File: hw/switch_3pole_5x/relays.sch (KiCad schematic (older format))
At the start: 31 parts, among them J1 WAGO 2081-1123, J2 WAGO 2081-1123, J3 WAGO 2081-1123, J4 WAGO 2081-1123, J5 WAGO 2081-1123, Q1 BSS138, Q2 BSS138, Q3 BSS138, Q4 BSS138, Q5 BSS138

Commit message: Added LED and testpoints
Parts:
- added D10, D6, D7, D8, D9: LED, LED:LED_RM2.54mm_D3mm, symbol standard:LED
- added J10: tp_relay_1, Connector_Miscelleaneus:Testpoint_1mm, symbol connectors:CONN_1
- added J11: tp_relay_2, Connector_Miscelleaneus:Testpoint_1mm, symbol connectors:CONN_1
- added J17: tp_relay_3, Connector_Miscelleaneus:Testpoint_1mm, symbol connectors:CONN_1
- added J18: tp_relay_4, Connector_Miscelleaneus:Testpoint_1mm, symbol connectors:CONN_1
- added J6: tp_relay_0, Connector_Miscelleaneus:Testpoint_1mm, symbol connectors:CONN_1
- added R12, R13, R14, R15, R6: 1k5, Resistor:R_0805, symbol standard:R
- D1, D2, D3, D4, D5: symbol D -> switch_3pole_5x-rescue:D
- J1, J2, J3, J4, J5: symbol CONN_3X1 -> switch_3pole_5x-rescue:CONN_3X1
- LOGO2: symbol OPEN_HARDWARE_1 -> switch_3pole_5x-rescue:OPEN_HARDWARE_1
- Q1, Q2, Q3, Q4, Q5: symbol BSS138 -> switch_3pole_5x-rescue:BSS138
- R1, R10, R11, R2, R3, R4, R5, R7, R8, R9: symbol R -> switch_3pole_5x-rescue:R
- REL1, REL2, REL3, REL4, REL5: symbol FINDER_34.51.7.024 -> switch_3pole_5x-rescue:FINDER_34.51.7.024
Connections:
- net GND: no longer R3.2
- net at D1.1 (A), Q1.3 (D), REL1.1 (+): now also D6.2 (C), J6.1
- net at D2.1 (A), Q2.3 (D), REL2.1 (+): now also D7.2 (C), J10.1
- net at D3.1 (A), Q3.3 (D), REL3.1 (+): now also D8.2 (C), J11.1
- net at D4.1 (A), Q4.3 (D), REL4.1 (+): now also D9.2 (C), J17.1
- net at D5.1 (A), Q5.3 (D), REL5.1 (+): now also D10.2 (C), J18.1
- new net: D6.1 (A), R6.1
- new net: D7.1 (A), R12.1
- new net: D8.1 (A), R13.1
- new net: D9.1 (A), R14.1
- new net: D10.1 (A), R15.1
- new net +5V: R12.2, R13.2, R14.2, R15.2, R6.2
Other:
- moved on the sheet: D1, D2, D3, D4, D5, J1, J2, J3, J4, J5, Q1, Q2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

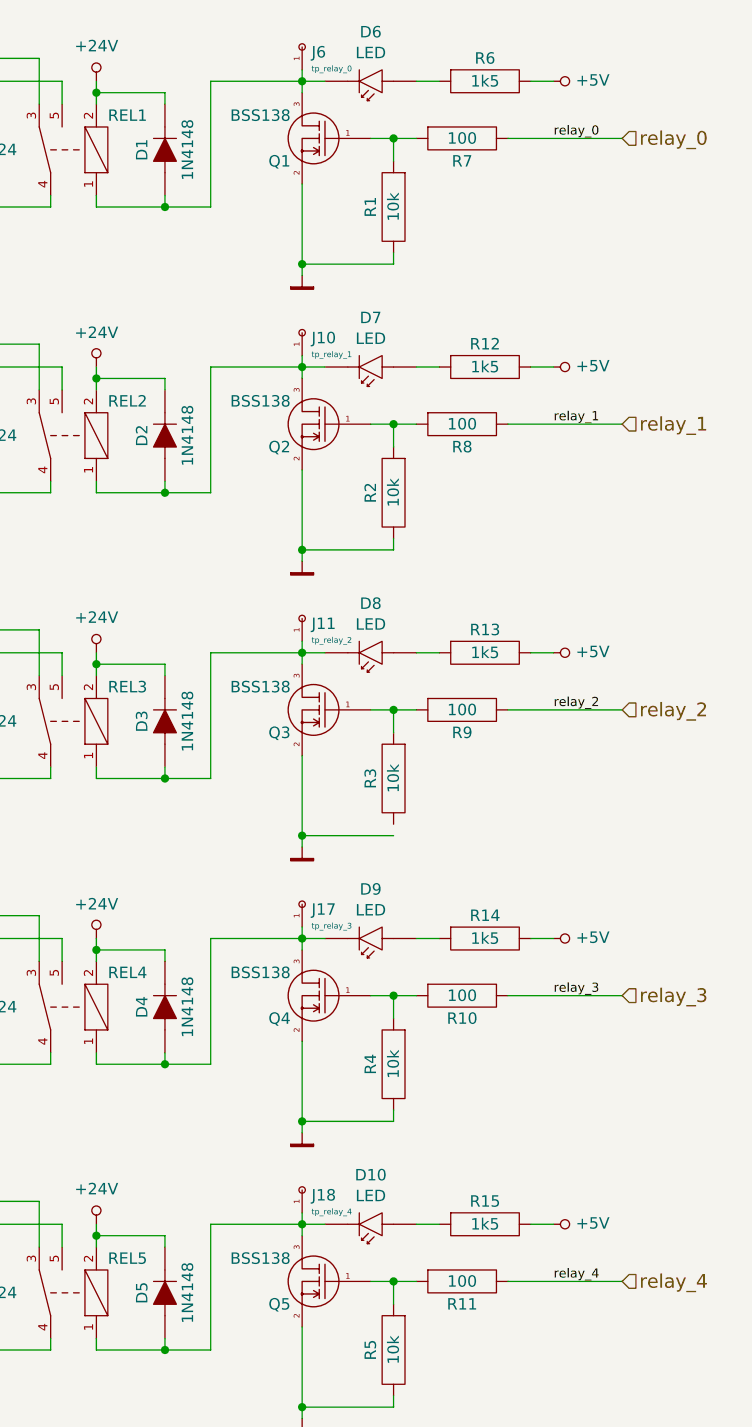
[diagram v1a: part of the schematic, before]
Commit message: added testpoints and LEDs updated 3d footprints
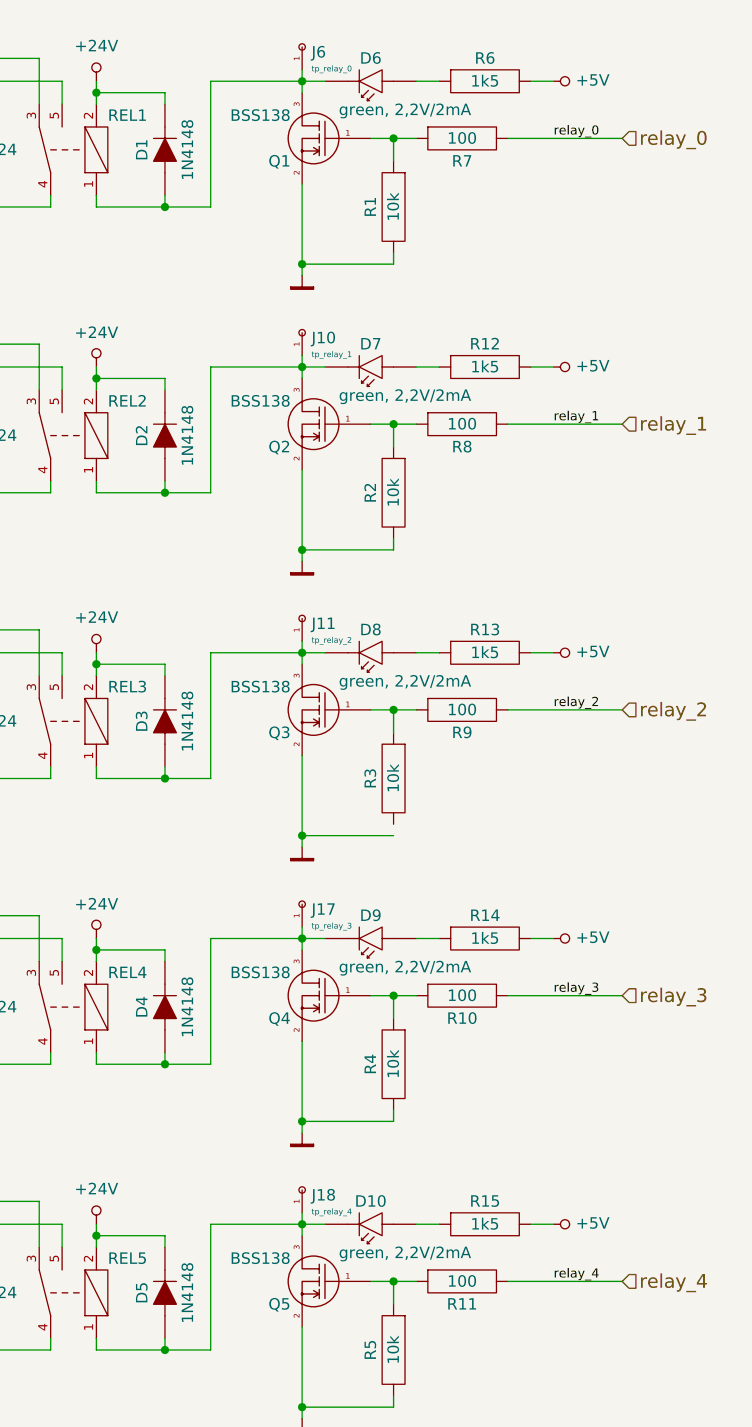
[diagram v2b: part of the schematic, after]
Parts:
- D10, D6, D7, D8, D9: value LED -> green, 2,2V/2mA
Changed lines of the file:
@@
 U 1 1 5BAE68FF
 P 6100 1050
-F 0 "D6" H 6300 985 50  0000 C CNN
-F 1 "LED" H 6300 1076 50  0000 C CNN
+F 0 "D6" H 6300 1100 50  0000 C CNN
+F 1 "green, 2,2V/2mA" H 6150 1325 50  0000 C CNN
 F 2 "LED:LED_RM2.54mm_D3mm" H 6100 1050 60  0001 C CNN
 F 3 "" H 6100 1050 60  0000 C CNN
@@
 U 1 1 5BAE6C7F
 P 6100 2300
-F 0 "D7" H 6300 2235 50  0000 C CNN
-F 1 "LED" H 6300 2326 50  0000 C CNN
+F 0 "D7" H 6300 2350 50  0000 C CNN
+F 1 "green, 2,2V/2mA" H 6150 2575 50  0000 C CNN
 F 2 "LED:LED_RM2.54mm_D3mm" H 6100 2300 60  0001 C CNN
 F 3 "" H 6100 2300 60  0000 C CNN
@@
 U 1 1 5BAE6E48
 P 6100 3550
-F 0 "D8" H 6300 3485 50  0000 C CNN
-F 1 "LED" H 6300 3576 50  0000 C CNN
+F 0 "D8" H 6300 3600 50  0000 C CNN
+F 1 "green, 2,2V/2mA" H 6150 3825 50  0000 C CNN
 F 2 "LED:LED_RM2.54mm_D3mm" H 6100 3550 60  0001 C CNN
 F 3 "" H 6100 3550 60  0000 C CNN
@@
 U 1 1 5BAE6FA0
 P 6100 4800
-F 0 "D9" H 6300 4735 50  0000 C CNN
-F 1 "LED" H 6300 4826 50  0000 C CNN
+F 0 "D9" H 6300 4850 50  0000 C CNN
+F 1 "green, 2,2V/2mA" H 6150 5075 50  0000 C CNN
 F 2 "LED:LED_RM2.54mm_D3mm" H 6100 4800 60  0001 C CNN
 F 3 "" H 6100 4800 60  0000 C CNN
@@
 U 1 1 5BAE7102
 P 6100 6050
-F 0 "D10" H 6300 5985 50  0000 C CNN
-F 1 "LED" H 6300 6076 50  0000 C CNN
+F 0 "D10" H 6300 6100 50  0000 C CNN
+F 1 "green, 2,2V/2mA" H 6150 6325 50  0000 C CNN
 F 2 "LED:LED_RM2.54mm_D3mm" H 6100 6050 60  0001 C CNN
 F 3 "" H 6100 6050 60  0000 C CNN

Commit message: fixed switch_3pole_5x library references added component placement drawings updated 3d images and gerber files
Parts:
- D1, D2, D3, D4, D5: symbol switch_3pole_5x-rescue:D -> standard:D
- J1, J2, J3, J4, J5: symbol switch_3pole_5x-rescue:CONN_3X1 -> connectors:CONN_3X1
- LOGO2: symbol switch_3pole_5x-rescue:OPEN_HARDWARE_1 -> logo:OPEN_HARDWARE_1
- Q1, Q2, Q3, Q4, Q5: symbol switch_3pole_5x-rescue:BSS138 -> transistors:BSS138
- R1, R10, R11, R2, R3, R4, R5, R7, R8, R9: symbol switch_3pole_5x-rescue:R -> standard:R
- REL1, REL2, REL3, REL4, REL5: symbol switch_3pole_5x-rescue:FINDER_34.51.7.024 -> relays:FINDER_34.51.7.024
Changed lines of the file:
@@
 Title "switch 3pole 5x (relays)"
 Date "2018-09-18"
-Rev "1"
+Rev "A"
 Comp "koewiba"
 Comment1 ""
@@
 $EndDescr
 $Comp
-L power1:+24V #PWR04
+L power:+24V #PWR04
 U 1 1 572DA356
 P 4700 2450
@@
 $EndComp
 $Comp
-L switch_3pole_5x-rescue:D D1
+L standard:D D1
 U 1 1 572DA3A8
 P 5000 1500
@@
 $EndComp
 $Comp
-L switch_3pole_5x-rescue:D D2
+L standard:D D2
 U 1 1 572DA4C3
 P 5000 2750
@@
 $EndComp
 $Comp
-L switch_3pole_5x-rescue:BSS138 Q2
+L transistors:BSS138 Q2
 U 1 1 572DAB4D
 P 5700 2700
@@
 $EndComp
 $Comp
-L switch_3pole_5x-rescue:BSS138 Q1
+L transistors:BSS138 Q1
 U 1 1 572DAC4A
 P 5700 1450
@@
 $EndComp
 $Comp
-L switch_3pole_5x-rescue:R R7
+L standard:R R7
 U 1 1 572DAC83
 P 6300 1450
@@
 $EndComp
 $Comp
-L switch_3pole_5x-rescue:R R1
+L standard:R R1
 U 1 1 572DAD70
 P 6000 1750
@@
 $EndComp
 $Comp
-L switch_3pole_5x-rescue:R R2
+L standard:R R2
 U 1 1 572DADE3
 P 6000 3000
@@
 $EndComp
 $Comp
-L switch_3pole_5x-rescue:R R8
+L standard:R R8
 U 1 1 572DAE46
 P 6300 2700
@@
 $EndComp
 $Comp
-L switch_3pole_5x-rescue:GND #PWR05
+L power:GND #PWR05
 U 1 1 572DB59F
 P 5600 3300
@@
 $EndComp
 $Comp
-L switch_3pole_5x-rescue:GND #PWR06
+L power:GND #PWR06
 U 1 1 572DB5CD
 P 5600 2050
@@
 relay_1
 $Comp
-L switch_3pole_5x-rescue:OPEN_HARDWARE_1 LOGO2
+L logo:OPEN_HARDWARE_1 LOGO2
 U 1 1 5B10FE77
 P 975 7350
@@
 RELAY_0_NC
 $Comp
-L switch_3pole_5x-rescue:FINDER_34.51.7.024 REL2
+L relays:FINDER_34.51.7.024 REL2
 U 1 1 5842EAE4
 P 4700 2750
@@
 $EndComp
 $Comp
-L switch_3pole_5x-rescue:FINDER_34.51.7.024 REL1
+L relays:FINDER_34.51.7.024 REL1
 U 1 1 5842E555
 P 4700 1500
@@
 Connection ~ 4700 1250
 $Comp
-L power1:+24V #PWR07
+L power:+24V #PWR07
 U 1 1 584354C0
 P 4700 1200
@@
 	5200 1200 5600 1200
 $Comp
-L power1:+24V #PWR08
+L power:+24V #PWR08
 U 1 1 5B0D5EB1
 P 4700 4950
@@
 $EndComp
 $Comp
-L switch_3pole_5x-rescue:D D3
+L standard:D D3
 U 1 1 5B0D5EB7
 P 5000 4000
@@
 $EndComp
 $Comp
-L switch_3pole_5x-rescue:D D4
+L standard:D D4
 U 1 1 5B0D5EBD
 P 5000 5250
@@
 $EndComp
 $Comp
-L switch_3pole_5x-rescue:BSS138 Q4
+L transistors:BSS138 Q4
 U 1 1 5B0D5EC3
 P 5700 5200
@@
 $EndComp
 $Comp
-L switch_3pole_5x-rescue:BSS138 Q3
+L transistors:BSS138 Q3
 U 1 1 5B0D5EC9
 P 5700 3950
@@
 $EndComp
 $Comp
-L switch_3pole_5x-rescue:R R9
+L standard:R R9
 U 1 1 5B0D5ECF
 P 6300 3950
@@
 $EndComp
 $Comp
-L switch_3pole_5x-rescue:R R3
+L standard:R R3
 U 1 1 5B0D5ED5
 P 6000 4250
@@
 $EndComp
 $Comp
-L switch_3pole_5x-rescue:R R4
+L standard:R R4
 U 1 1 5B0D5EDB
 P 6000 5500
@@
 $EndComp
 $Comp
-L switch_3pole_5x-rescue:R R10
+L standard:R R10
 U 1 1 5B0D5EE1
 P 6300 5200
@@
 $EndComp
 $Comp
-L switch_3pole_5x-rescue:GND #PWR09
+L power:GND #PWR09
 U 1 1 5B0D5EE7
 P 5600 5800
@@
 $EndComp
 $Comp
-L switch_3pole_5x-rescue:GND #PWR010
+L power:GND #PWR010
 U 1 1 5B0D5EED
 P 5600 4550
@@
 relay_3
 $Comp
-L switch_3pole_5x-rescue:FINDER_34.51.7.024 REL4
+L relays:FINDER_34.51.7.024 REL4
 U 1 1 5B0D5EF8
 P 4700 5250
@@
 $EndComp
 $Comp
-L switch_3pole_5x-rescue:FINDER_34.51.7.024 REL3
+L relays:FINDER_34.51.7.024 REL3
 U 1 1 5B0D5EFE
 P 4700 4000
@@
 Connection ~ 4700 3750
 $Comp
-L power1:+24V #PWR011
+L power:+24V #PWR011
 U 1 1 5B0D5F25
 P 4700 3700
@@
 	5200 3700 5600 3700
 $Comp
-L switch_3pole_5x-rescue:D D5
+L standard:D D5
 U 1 1 5B0D679E
 P 5000 6500
@@
 $EndComp
 $Comp
-L switch_3pole_5x-rescue:BSS138 Q5
+L transistors:BSS138 Q5
 U 1 1 5B0D67B0
 P 5700 6450
@@
 $EndComp
 $Comp
-L switch_3pole_5x-rescue:R R11
+L standard:R R11
 U 1 1 5B0D67B6
 P 6300 6450
@@
 $EndComp
 $Comp
-L switch_3pole_5x-rescue:R R5
+L standard:R R5
 U 1 1 5B0D67BC
 P 6000 6750
@@
 $EndComp
 $Comp
-L switch_3pole_5x-rescue:GND #PWR012
+L power:GND #PWR012
 U 1 1 5B0D67D4
 P 5600 7050
@@
 relay_4
 $Comp
-L switch_3pole_5x-rescue:FINDER_34.51.7.024 REL5
+L relays:FINDER_34.51.7.024 REL5
 U 1 1 5B0D67E5
 P 4700 6500
@@
 Connection ~ 4700 6250
 $Comp
-L power1:+24V #PWR013
+L power:+24V #PWR013
 U 1 1 5B0D680C
 P 4700 6200
@@
 	6500 5200 7000 5200
 $Comp
-L switch_3pole_5x-rescue:CONN_3X1 J1
+L connectors:CONN_3X1 J1
 U 1 1 5B1A6C69
 P 3250 1200
@@
 RELAY_1_NC
 $Comp
-L switch_3pole_5x-rescue:CONN_3X1 J2
+L connectors:CONN_3X1 J2
 U 1 1 5B1A7334
 P 3250 2450
@@
 RELAY_2_NC
 $Comp
-L switch_3pole_5x-rescue:CONN_3X1 J3
+L connectors:CONN_3X1 J3
 U 1 1 5B1A79FD
 P 3250 3700
@@
 RELAY_3_NC
 $Comp
-L switch_3pole_5x-rescue:CONN_3X1 J4
+L connectors:CONN_3X1 J4
 U 1 1 5B1A7AE1
 P 3250 4950
@@
 RELAY_4_NC
 $Comp
-L switch_3pole_5x-rescue:CONN_3X1 J5
+L connectors:CONN_3X1 J5
 U 1 1 5B1A7B8A
 P 3250 6200
